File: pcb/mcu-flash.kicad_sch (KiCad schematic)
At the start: 26 parts, among them J1 0015910100, SW1 SW_MEC_5E, U1 W25Q128JVS, U2 RP2040, Y1 ABM8AIG-12.000MHZ-12-2Z-T3

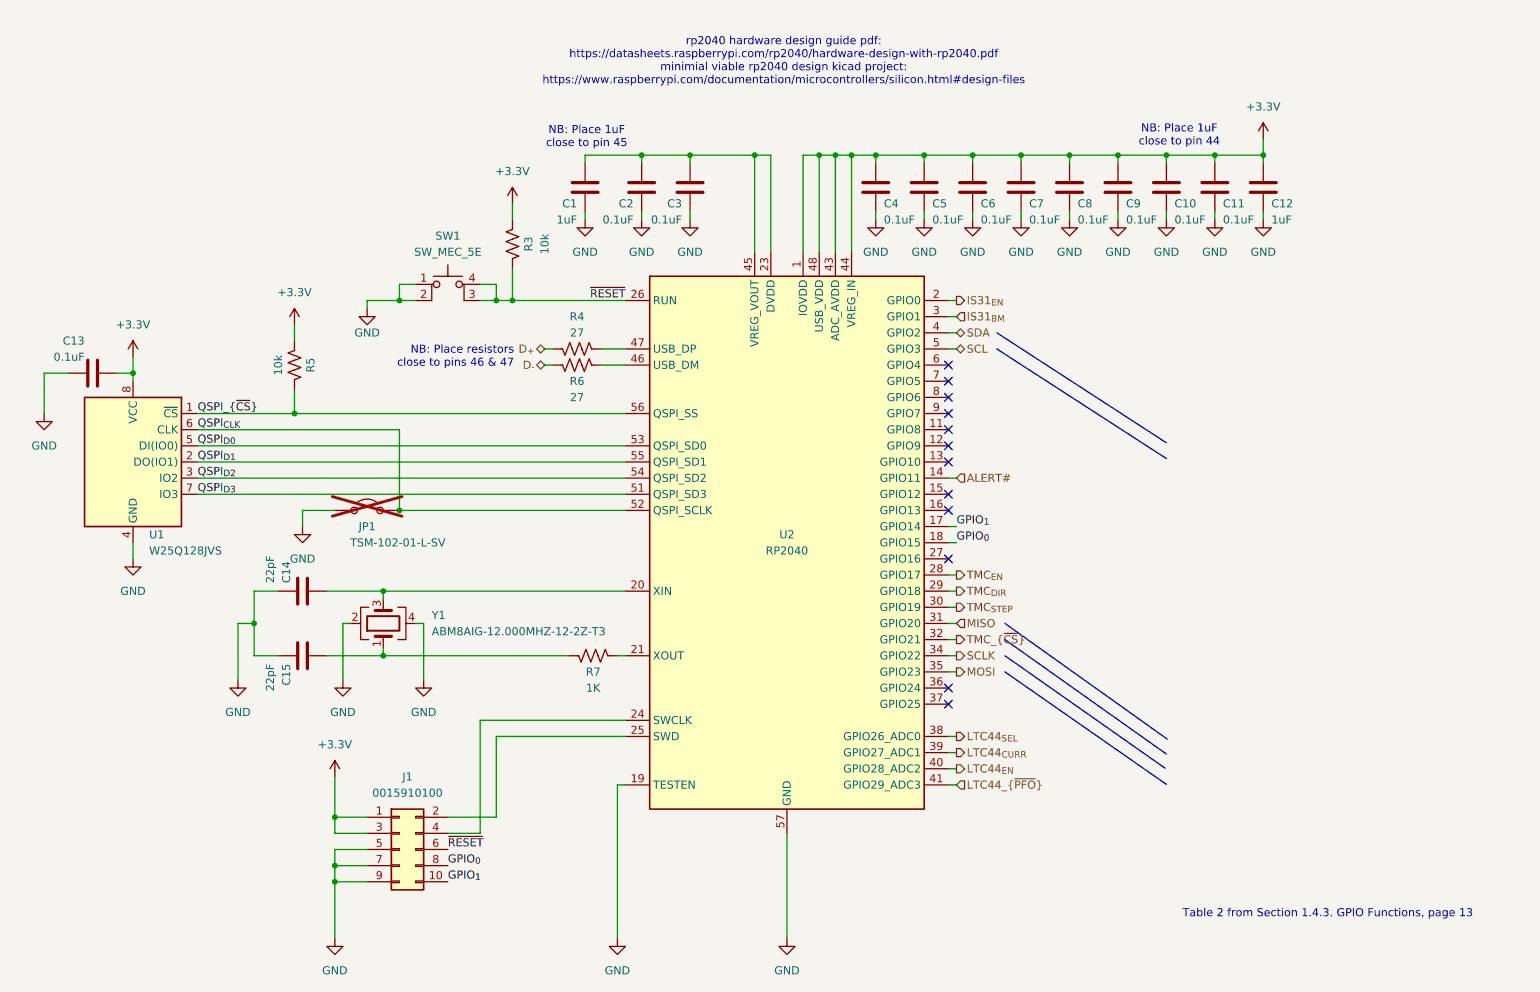
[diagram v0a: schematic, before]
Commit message: Revision E
- Resolve issues 1-11
- Add pdf of rev d schematic for easy comparison
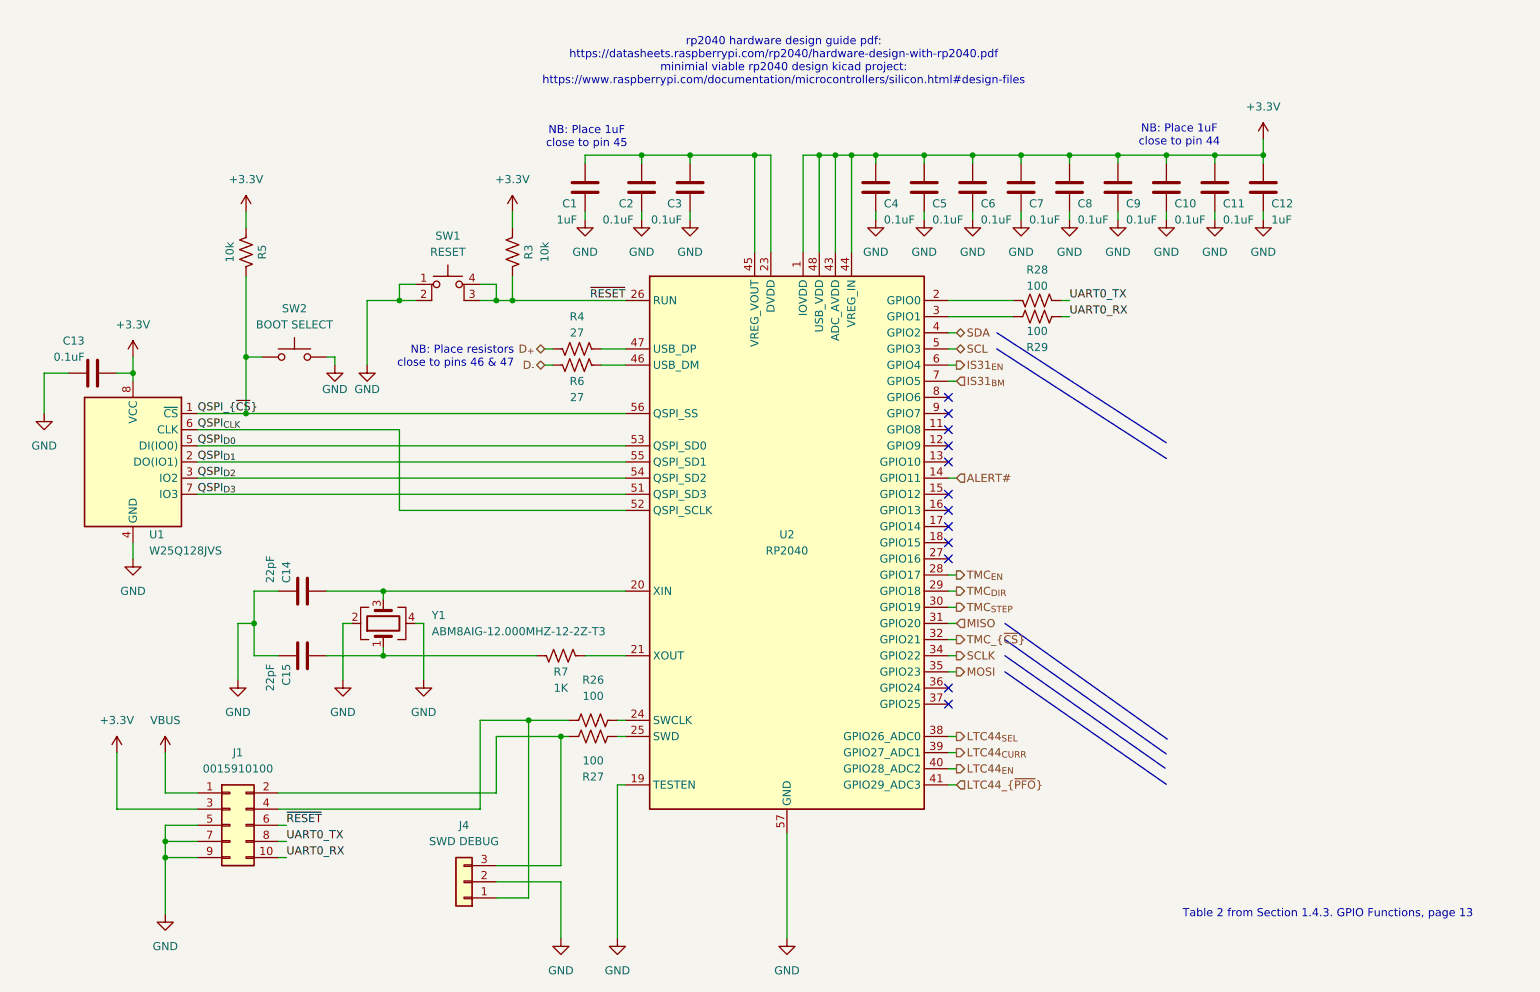
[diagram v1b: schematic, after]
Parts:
- removed JP1: TSM-102-01-L-SV, Connector_PinHeader_2.54mm:PinHeader_1x02_P2.54mm_Vertical_SMD_Pin1Left, symbol Jumper:Jumper_2_Open
- added J4: SWD DEBUG, Connector_JST:JST_SH_BM03B-SRSS-TB_1x03-1MP_P1.00mm_Vertical, symbol Connector_Generic:Conn_01x03
- added R26, R27, R28, R29: 100, Resistor_SMD:R_0402_1005Metric, symbol Device:R_US
- added SW2: BOOT SELECT, Button_Switch_SMD:SW_Push_1P1T_NO_6x6mm_H9.5mm, symbol Switch:SW_Push
- R3, R5: footprint Resistor_SMD:R_0402_1005Metric -> Resistor_SMD:R_0603_1608Metric
- SW1: value SW_MEC_5E -> RESET
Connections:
- net +3.3V: no longer J1.1 (Pin_1)
- net GND: now also J4.2 (Pin_2), SW2.2
- net IS31_{BM}: now also U2.7 (GPIO5); no longer U2.3 (GPIO1)
- net IS31_{EN}: now also U2.6 (GPIO4); no longer U2.2 (GPIO0)
- net QSPI_{~{CS}}: now also SW2.1
- net at J1.4 (Pin_4): now also J4.1 (Pin_1), R26.1; no longer U2.24 (SWCLK)
- net at U2.25 (SWD): now also R27.1; no longer J1.2 (Pin_2)
- net GPIO_{0}: no longer names the net of U2.18 (GPIO15)
- net GPIO_{0}: no longer J1.8 (Pin_8)
- net GPIO_{1}: no longer names the net of U2.17 (GPIO14)
- net GPIO_{1}: no longer J1.10 (Pin_10)
- new net: R26.2, U2.24 (SWCLK)
- new net: R28.2, U2.2 (GPIO0)
- new net: R29.2, U2.3 (GPIO1)
- new net: J1.2 (Pin_2), J4.3 (Pin_3), R27.2
- new net UART0_RX: J1.10 (Pin_10), R29.1
- new net UART0_TX: J1.8 (Pin_8), R28.1
- new net VBUS: J1.1 (Pin_1)
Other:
- moved on the sheet: J1, R3, R5, R7

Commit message: Address schematic and PCB issues for Rev. E
- Some layout alternations
- Some schematic cleanup
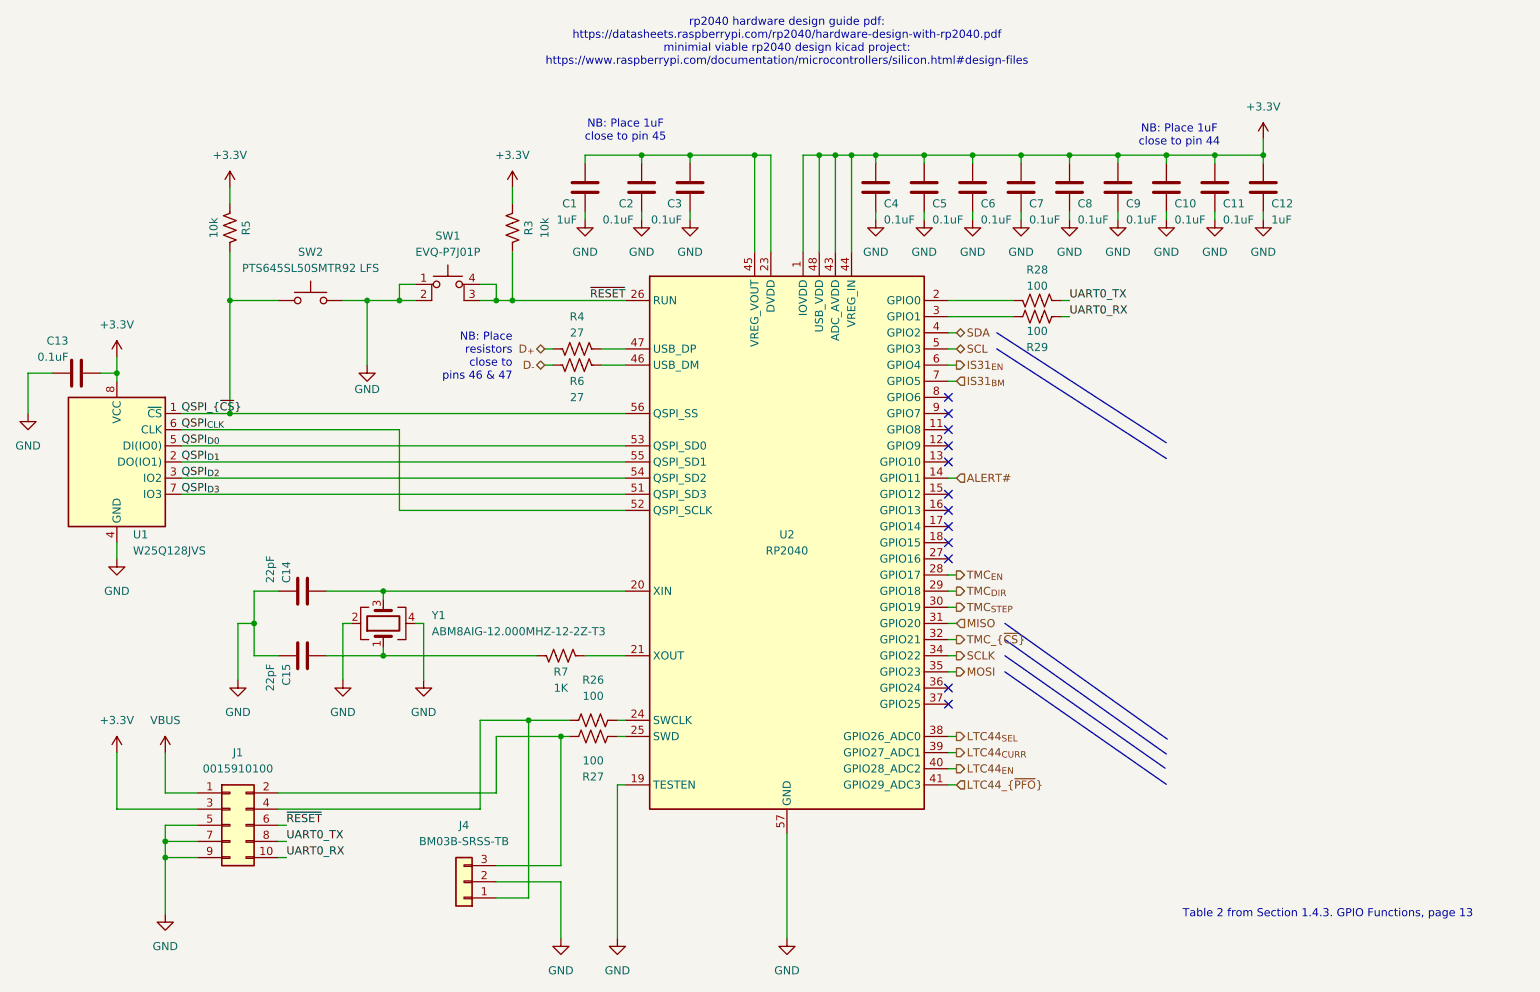
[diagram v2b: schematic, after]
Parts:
- J4: value SWD DEBUG -> BM03B-SRSS-TB
- SW1: value RESET -> EVQ-P7J01P
- SW2: value BOOT SELECT -> PTS645SL50SMTR92 LFS; footprint Button_Switch_SMD:SW_Push_1P1T_NO_6x6mm_H9.5mm -> Button_Switch_SMD:SW_SPST_PTS645
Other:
- moved on the sheet: C13, R3, R5, SW2, U1

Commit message: Removed GND plane back layer
- Moved the UART traces a little out of the way of xtal trace
- Labelled debug headers as DNP
- Changed i2c pull-ups back to 4.7k how they were in rev d. I
  changed these by mistake in commit 8da4fdf when reducing BOM component list
- Generated production files - ibom, gerber, drill files
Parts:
- J1, J4: now not fitted
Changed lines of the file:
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@@
 		(in_bom yes)
 		(on_board yes)
-		(dnp no)
+		(dnp yes)
 		(fields_autoplaced yes)
 		(property "Reference" "J1"
@@
 		(in_bom yes)
 		(on_board yes)
-		(dnp no)
+		(dnp yes)
 		(fields_autoplaced yes)
 		(property "Reference" "J4"

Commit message: Revision F Edits
- Reduce base capacitance
  - Reduce infill {width, gap}: {0.35, 1} -> {0.2, 1.2}
    - Equivalent to: 45.1% -> 26.5%
  - Entirely remove copper on 3rd (in2.Cu) layer
  - Reduce via count
- export rev e schematic to pdf
- put pdfs into manufacturing folder
- Fix 6mm tactile switch footprint
- Put gold under logo
- Increment schematic, pcb, and silkscreen revision to F
- Add labels to debug header
- Add 10k pull-up to tmc2130 enable pin
- Convert all symbols & footprints library aliases from "oe" to "open-ephys"
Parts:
- SW1: footprint oe:PANASONIC_EVQP7-JA-01P -> open-ephys:PANASONIC_EVQP7-JA-01P
- SW2: value PTS645SL50SMTR92 LFS -> TS04-66-50-BK-160-SMT; footprint Button_Switch_SMD:SW_SPST_PTS645 -> open-ephys:SAMESKY-TS04-66-XX-BK-XXX-SMT-XX
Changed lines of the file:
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@@
 			)
 		)
-		(property "Value" "PTS645SL50SMTR92 LFS"
+		(property "Value" "TS04-66-50-BK-160-SMT"
 			(at 67.31 58.42 0)
 			(effects
@@
 			)
 		)
-		(property "Footprint" "Button_Switch_SMD:SW_SPST_PTS645"
+		(property "Footprint" "open-ephys:SAMESKY-TS04-66-XX-BK-XXX-SMT-XX"
 			(at 67.31 58.42 0)
 			(effects
@@
 			)
 		)
-		(property "Datasheet" "https://www.ckswitches.com/media/1471/pts645.pdf"
+		(property "Datasheet" "~"
 			(at 67.31 58.42 0)
 			(effects
@@
 			)
 		)
-		(property "Footprint" "oe:PANASONIC_EVQP7-JA-01P"
+		(property "Footprint" "open-ephys:PANASONIC_EVQP7-JA-01P"
 			(at 88.9 55.88 0)
 			(effects
@@
 			)
 		)
-		(property "Datasheet" "https://api.pim.na.industrial.panasonic.com/file_stream/main/fileversion/245500"
+		(property "Datasheet" "http://www.apem.com/int/index.php?controller=attachment&id_attachment=1371"
 			(at 88.9 55.88 0)
 			(effects

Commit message: Some edits during PR review
- Silkscreen moved on board
- Get rid of value text in fab layer
- Invert TMC_EN name to indicate correct logic
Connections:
- net TMC_{EN} renamed TMC_{~{EN}}
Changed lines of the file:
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@@
 		)
 	)
-	(hierarchical_label "TMC_{EN}"
+	(hierarchical_label "TMC_{~{EN}}"
 		(shape output)
 		(at 168.91 106.68 0)

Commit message: Revision G edits
- Move R10 & R13 silk screen designators closer to their respective
  resistors
- Add specific part numbers to C15 & C15 which are xtal caps w/ NP0 temp
  coefficient
- Update libraries to remove solder paste from big caps' footprint
- Made boot select button footprint to datasheet spec (had to move some
  traces to do this)
- Remove solder paste from LED footprint
- Update revision f-->g in sch, pcb, & pcb's silk screen
- No solder paste in the LED footprint
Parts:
- C14, C15: value 22pF -> C0402C0G500-220GNP-CT
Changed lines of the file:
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@@
 	)
 	(hierarchical_label "LTC44_{CURR}"
-		(shape output)
+		(shape input)
 		(at 168.91 134.62 0)
 		(fields_autoplaced yes)
@@
 			)
 		)
-		(property "Datasheet" "http://www.winbond.com/resource-files/w25q128jv_dtr%20revc%2003272018%20plus.pdf"
+		(property "Datasheet" "https://www.winbond.com/resource-files/w25q128jv_dtr%20revc%2003272018%20plus.pdf"
 			(at 36.83 88.9 0)
 			(effects
@@
 			)
 		)
-		(property "Value" "22pF"
+		(property "Value" "C0402C0G500-220GNP-CT"
 			(at 60.96 107.95 0)
 			(effects
@@
 			)
 		)
-		(property "Value" "22pF"
+		(property "Value" "C0402C0G500-220GNP-CT"
 			(at 60.96 120.65 0)
 			(effects
